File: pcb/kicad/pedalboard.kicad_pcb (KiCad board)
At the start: 4 copper layers, 208 x 90 mm, 228 parts, among them J1 Pi 5 GPIO header, J10 Switch 2, J11 Switch 3, J12 Switch 4, J13 Switch 5, J14 Switch 6, J15 Switch 7, J16 Switch 8, J17 Expression, J18 MIDI out, J2 Screen PH2.0, J3 Screen 5V/GND pins, J4 To Pi 5 J2 pads, J5 Guitar in, J6 Main out L, J7 Main out R, J8 Headphones, J9 Switch 1, Q1 BC857, SW1 Power, U1 TLV75733PDBV, U10 LM393B, U11 OPA1642AIDR, U12 TPA6130A2RTJR, U13 SRV05-4, U14 SRV05-4, U15 SRV05-4, U16 SRV05-4, U17 SRV05-4, U2 TPS7A2033PDBV, U3 TPS61040DBV, U4 TPS7A4901DGN, U5 CAT24C32WI-GT3, U6 PCM5122PW, U7 74LVC1G32, U8 PCM1863DBT, U9 OPA1642AIDR, Y1 22.5792MHz, Y2 24.576MHz

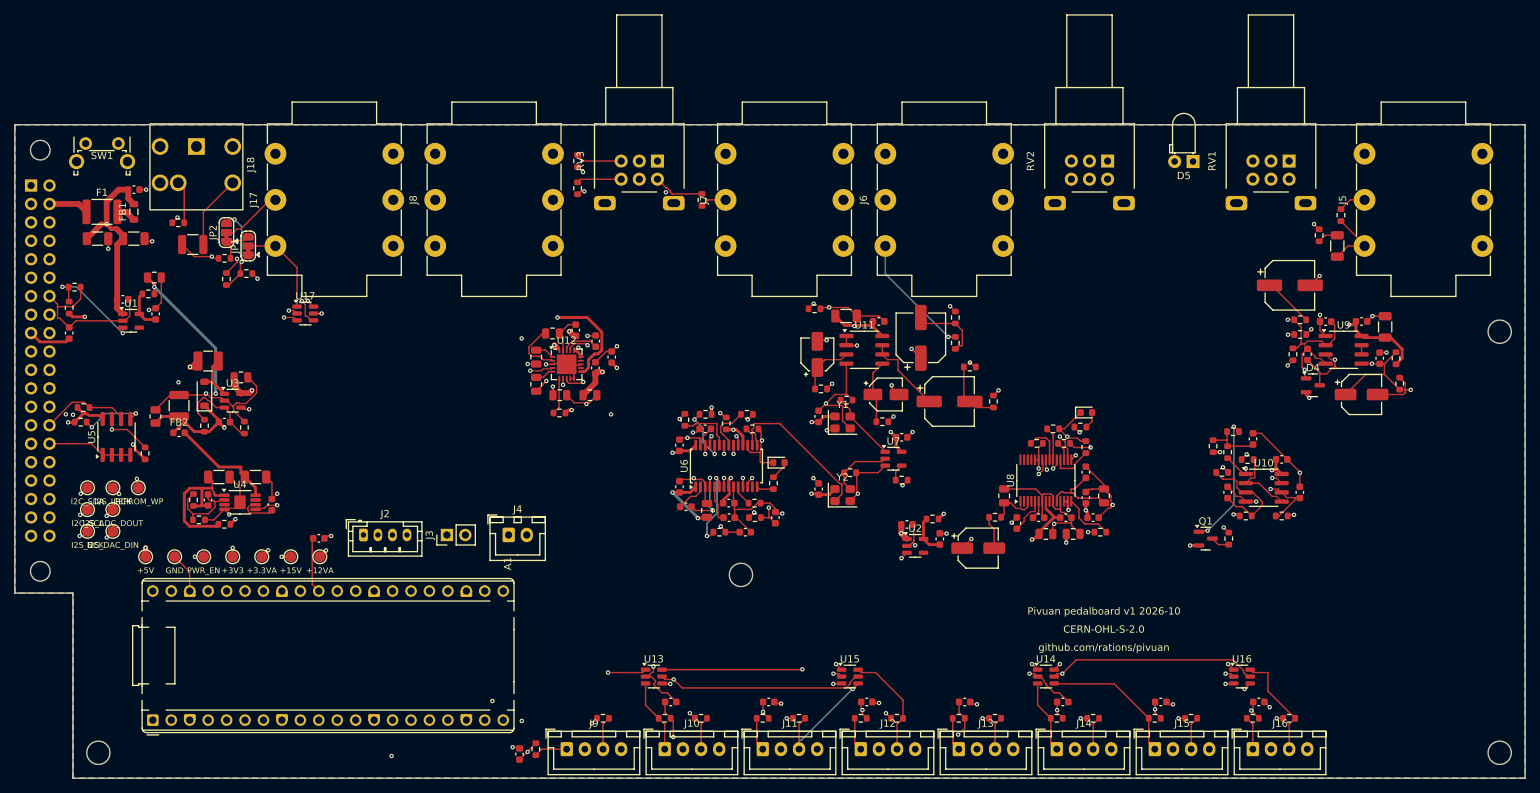
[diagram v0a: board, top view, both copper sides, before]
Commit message: Pedalboard PCB: board fully routed
Every net is connected and KiCad's DRC shows no clearance or connection
errors; only silkscreen warnings are left. Each surface-mount ground pad
has its own via to the In1 ground plane, the router is kept off that
plane, the headphone amplifier's capacitors sit in line with its pins,
and the top and bottom layers have ground pours. Net classes: 5 V input
0.8 mm, supplies 0.4 mm, headphone outputs 0.3 mm, signals 0.2 mm.

Co-Authored-By: Claude Opus 5.5 <noreply@anthropic.com>
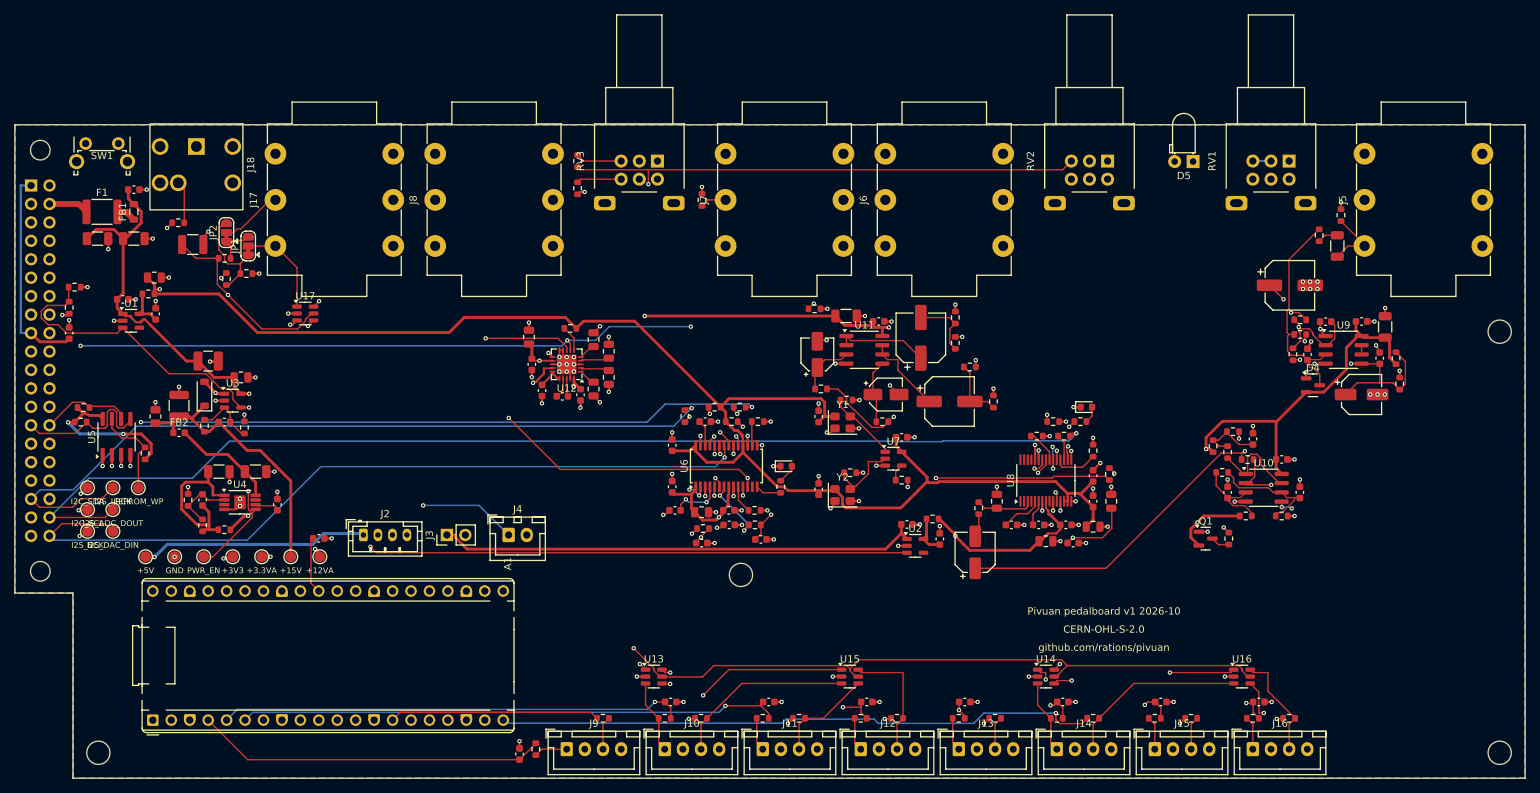
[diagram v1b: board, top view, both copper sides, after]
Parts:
- moved R58 11.7 mm to (106.5, 58.0)
- moved C64 11.6 mm to (100.8, 59.2), turned to 90 degrees
- moved C66 10.6 mm to (102.6, 66.6), turned to -90 degrees
- moved C60 10.0 mm to (109.7, 59.6), turned to -90 degrees
- moved C36 9.91 mm to (175.8, 87.6), turned to 0 degrees
- moved C59 9.83 mm to (111.8, 64.8), turned to -90 degrees
- moved C61 9.06 mm to (111.8, 61.2), turned to 90 degrees
- moved C58 9.04 mm to (109.7, 66.4)
- moved C63 8.92 mm to (107.9, 67.2), turned to -90 degrees
- moved C65 8.88 mm to (105.4, 67.4), turned to 180 degrees
- moved C62 8.76 mm to (101.2, 63.0), turned to -90 degrees
- moved R26 8.10 mm to (180.8, 78.1), turned to 90 degrees
- moved C24 6.18 mm to (124.6, 87.6)
- moved C35 5.75 mm to (178.5, 78.4), turned to 90 degrees
- moved R8 3.72 mm to (55.9, 85.2)
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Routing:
- net GND: track 315.4 -> 129.0 mm, vias 49 -> 130
- net /Footswitch controller/MIDI_TX: track 1.01 -> 70.5 mm
- net I2C_SCL: track 201.8 -> 235.0 mm, vias 6 -> 5
- net +12VA: track 264.5 -> 235.5 mm, vias 10 -> 6
- net /Outputs/HP_L_OUT: track 0.00 -> 28.6 mm, vias 0 -> 1
- net /Footswitch controller/PICO_3V3: track 253.3 -> 226.8 mm, vias 4 -> 2
- net +5V: track 249.9 -> 227.3 mm, vias 8 -> 4
- net PI_3V3: track 56.6 -> 74.0 mm
- net /Pi header and connectors/PWR_BTN_B: track 86.9 -> 102.8 mm
- net VREF_5V: track 109.1 -> 125.0 mm, vias 4 -> 3
- net I2S_BCK: track 183.2 -> 198.4 mm
- net /Outputs/MAIN_R_W: track 41.4 -> 56.1 mm
- net +3V3: track 228.0 -> 242.5 mm, vias 13 -> 2
- net I2C_SDA: track 194.4 -> 206.8 mm, vias 5 -> 6
- net DAC_OUTL: track 138.7 -> 126.8 mm
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
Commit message: Pedalboard PCB: silkscreen tidied, test points relabeled
Labels clear of pads and other silkscreen, rear-part outlines clipped inside
the board edge, test points with short names above their pads (the header
ones in two rows), and a starved thermal on RV3 made solid. Rerouted.

Co-Authored-By: Claude Opus 5.5 <noreply@anthropic.com>
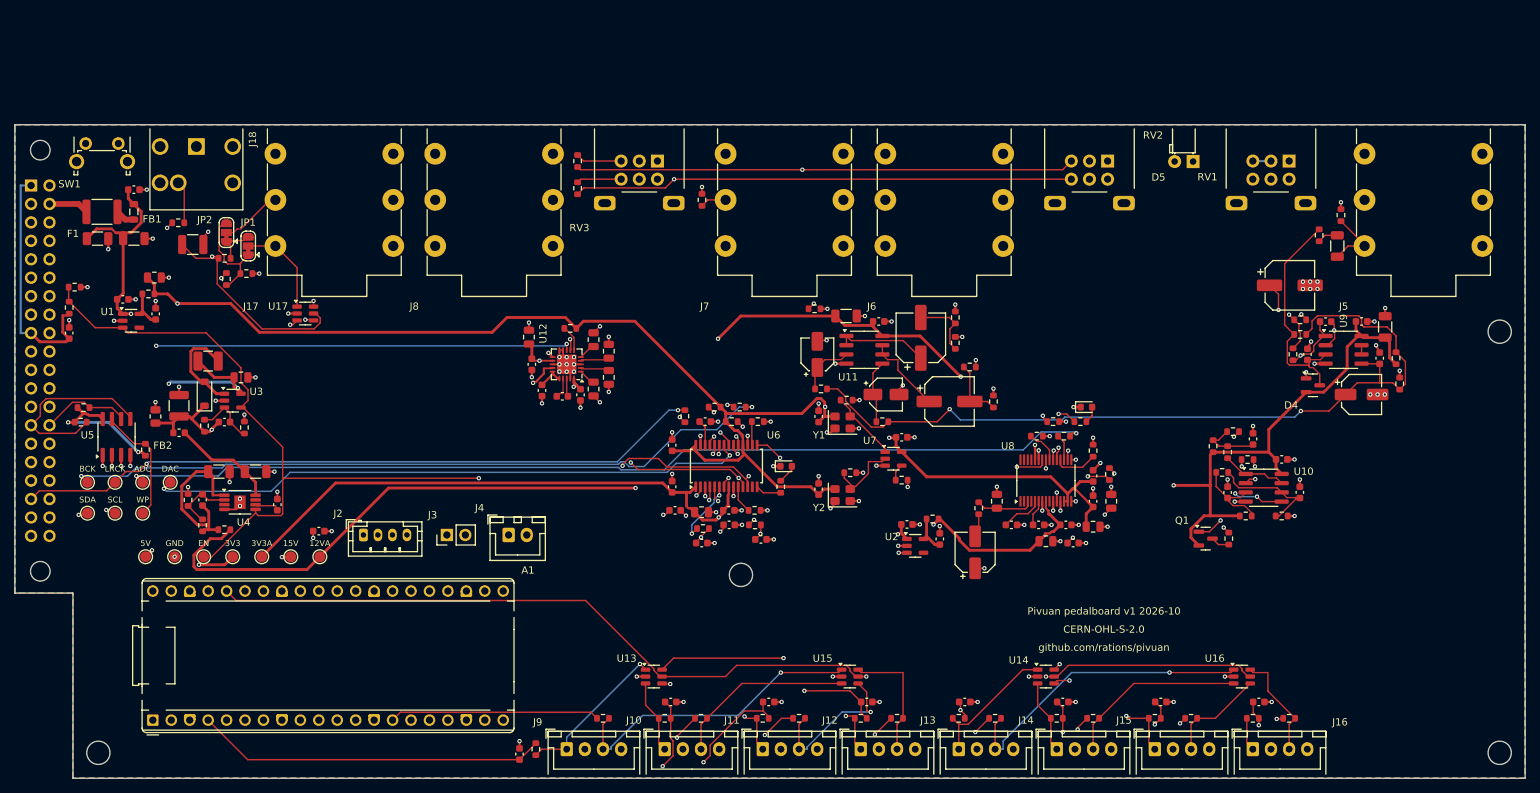
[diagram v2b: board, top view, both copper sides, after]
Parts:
- moved TP13 10.4 mm to (51.4, 79.2)
- moved TP10 6.75 mm to (40.0, 79.2)
- moved TP12 5.56 mm to (47.6, 79.2)
- moved TP9 3.83 mm to (43.8, 83.5)
- moved TP14 3.55 mm to (47.6, 83.5)
- moved TP8 3.50 mm to (40.0, 83.5)
- moved C75 1.00 mm to (71.9, 86.0)
- moved TP11 0.81 mm to (43.8, 79.2)
- moved R13 0.50 mm to (48.0, 74.8)
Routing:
- net I2C_SCL: track 235.0 -> 200.5 mm, vias 5 -> 6
- net I2C_SDA: track 206.8 -> 238.6 mm, vias 6 -> 5
- net DAC_OUTL: track 126.8 -> 149.7 mm
- net I2S_BCK: track 198.4 -> 180.7 mm, vias 4 -> 3
- net /Pi header and connectors/PWR_BTN_A: track 87.1 -> 103.4 mm, vias 1 -> 0
- net ADC_DRIVE: track 95.1 -> 109.6 mm
- net +3.3VA: track 146.1 -> 132.9 mm, vias 3 -> 2
- net /Outputs/MAIN_R_W: track 56.1 -> 44.9 mm
- net I2S_LRCK: track 170.1 -> 159.2 mm, vias 2 -> 3
- net VREF_5V: track 125.0 -> 114.6 mm, vias 3 -> 2
- net /Pi header and connectors/PWR_BTN_B: track 102.8 -> 93.8 mm
- net /Footswitch controller/FS2: track 64.0 -> 72.6 mm
- net /Footswitch controller/LED5_EXT: track 51.1 -> 42.6 mm
- net /Footswitch controller/LED7_EXT: track 22.0 -> 13.9 mm, vias 1 -> 0
- net DAC_OUTR: track 126.8 -> 135.0 mm
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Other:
- board text added: "12VA"
- board text added: "15V"
- board text added: "3V3"
- board text added: "3V3A"
- board text added: "5V"
- board text added: "ADC"
- board text added: "BCK"
- board text added: "DAC"
- board text added: "EN"
- board text added: "LRCK"
- board text added: "SCL"
- board text added: "SDA"
- board text added: "WP"
- board text removed: "+12VA"
- board text removed: "+15V"
- board text removed: "+3.3VA"
- board text removed: "+3V3"
- board text removed: "+5V"
- board text removed: "EEPROM_WP"
- board text removed: "I2C_SCL"
- board text removed: "I2C_SDA"
- board text removed: "I2S_ADC_DOUT"
- board text removed: "I2S_BCK"
- board text removed: "I2S_DAC_DIN"
- board text removed: "I2S_LRCK"
- board text removed: "PWR_EN"

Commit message: Pedalboard PCB: maker part numbers and LCSC numbers on every part
Each part on the schematic and the board now carries Manufacturer, MPN
and LCSC fields, for the PCBWay and JLCPCB assembly BOMs. FB1 is the
2 A bead (no 0805 bead is rated 3 A), F1 the MF-MSMF150-2 fuse. The
drill/place origin is the board's bottom-left corner, so the Gerbers,
drill and placement files measure from the board.

Co-Authored-By: Claude Opus 5.5 <noreply@anthropic.com>
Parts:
- FB1: value 220R@100MHz 3A -> 220R@100MHz 2A
